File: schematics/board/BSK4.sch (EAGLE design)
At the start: 19 parts

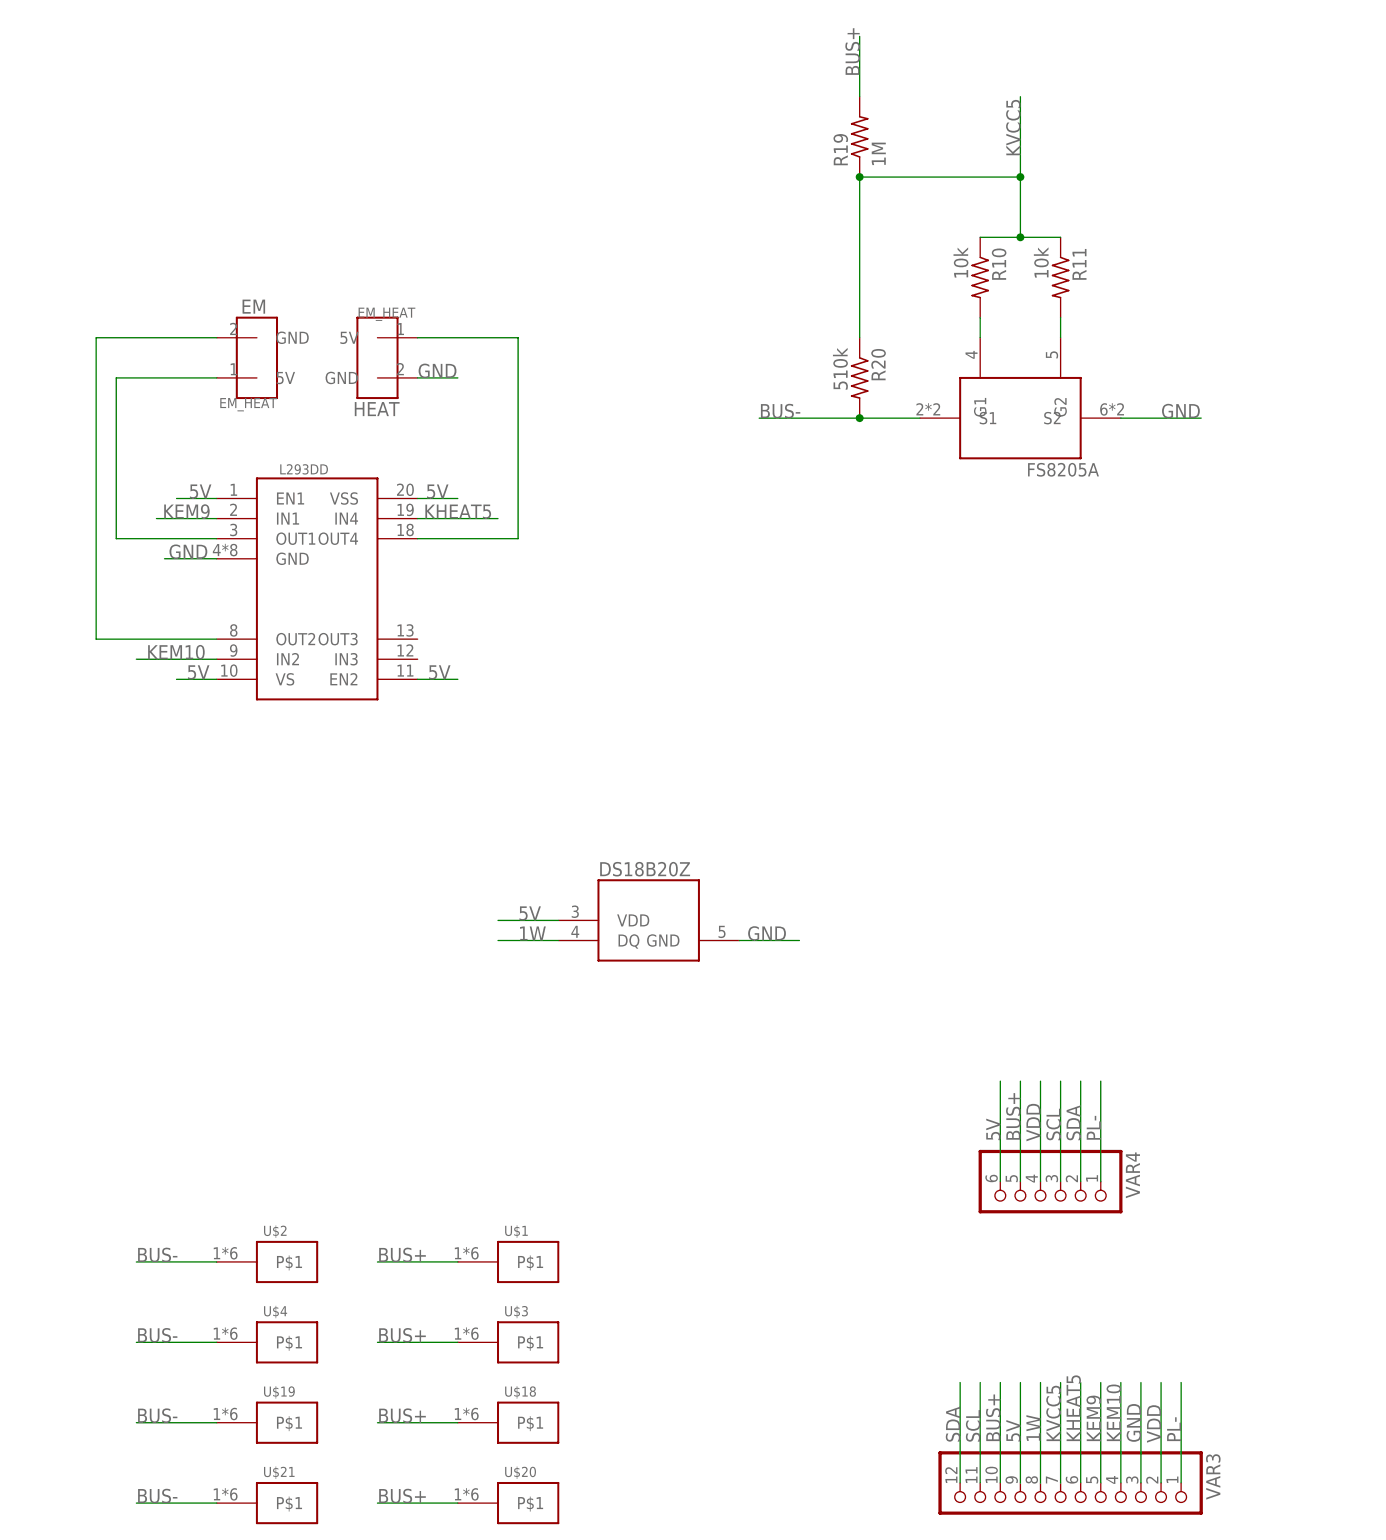
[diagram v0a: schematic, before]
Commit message: изменен БСК4
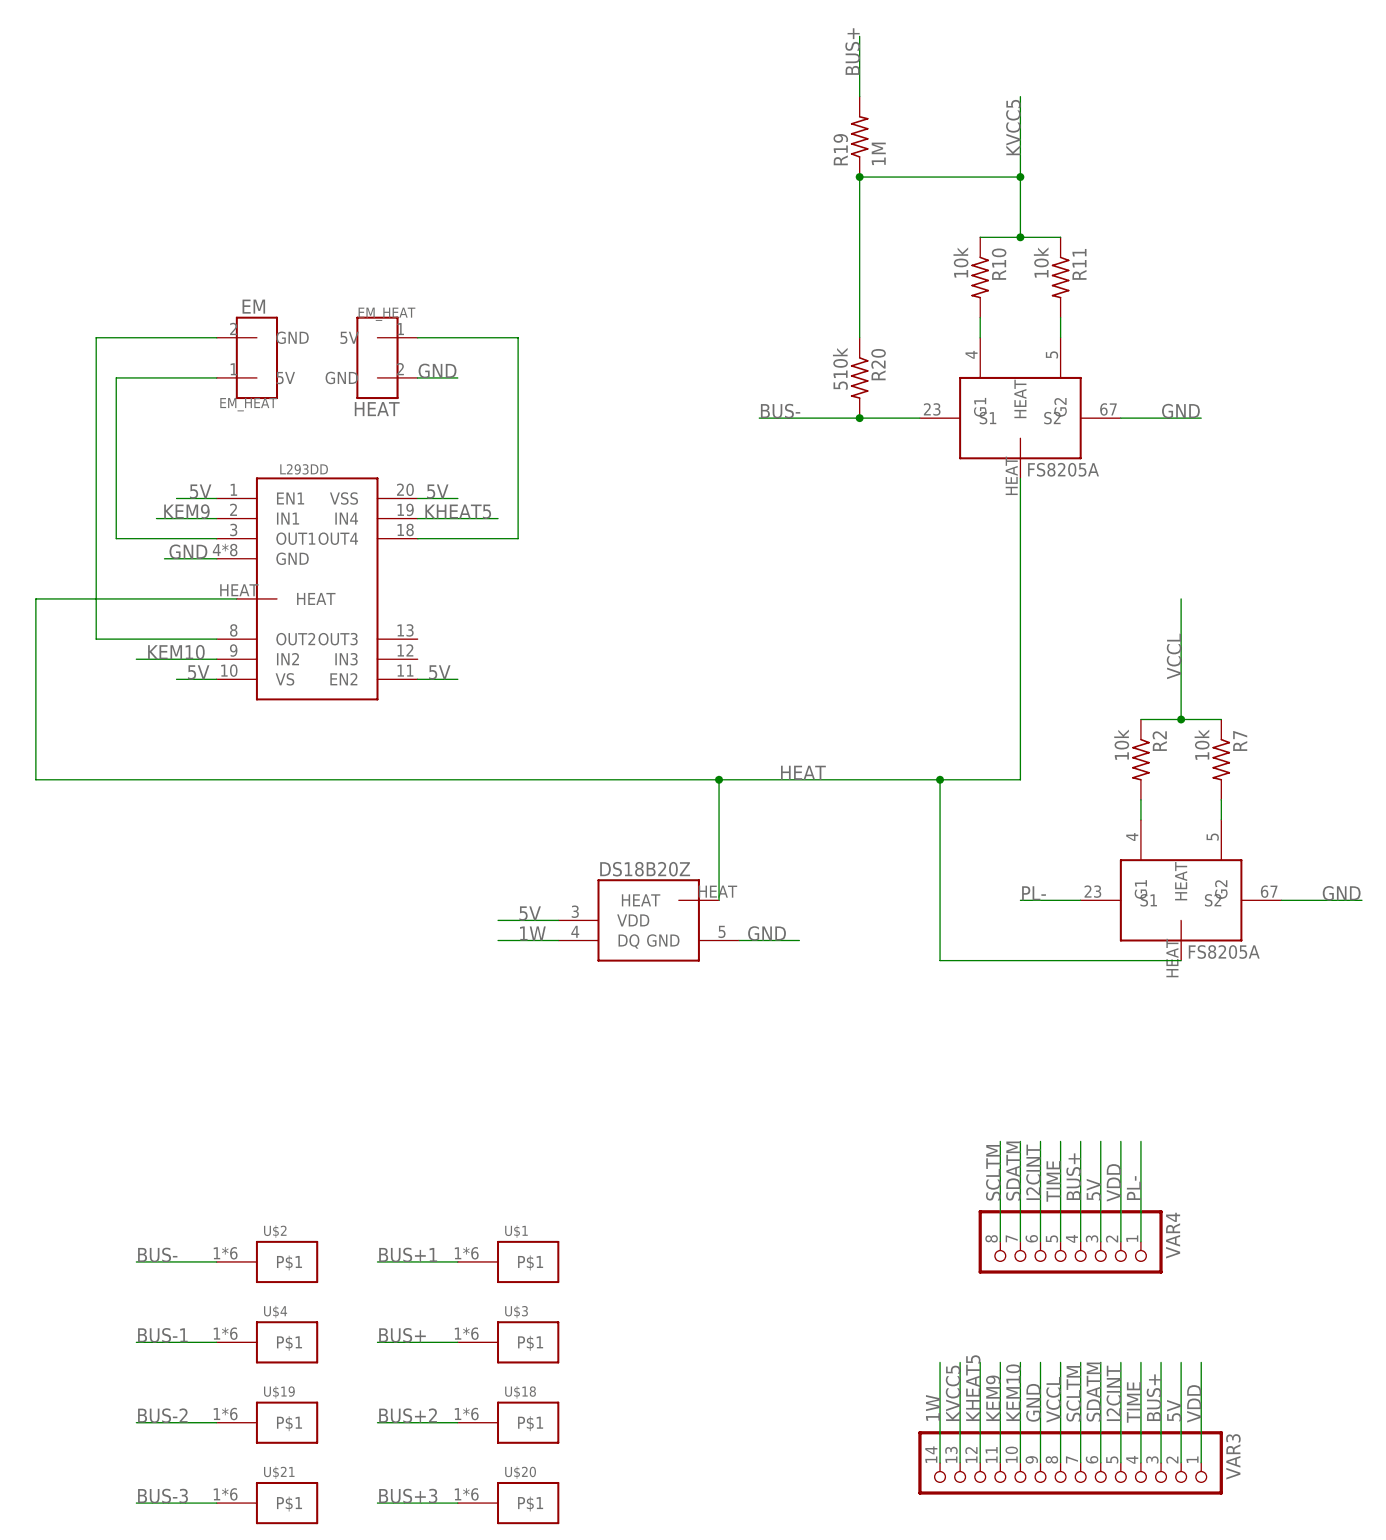
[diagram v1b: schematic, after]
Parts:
- removed U$14: FS8205A, CanCubeSat:FS8205A
- added R2, R7: 10k, resistor:R-US_R0603
- added U$10, U$9: FS8205A+, CanCubeSat:FS8205A+
- U$5: value DS18B20ZDS18B20Z -> DS18B20Z; device CanCubeSat:DS18B20ZDS18B20Z -> CanCubeSat:DS18B20Z
- VAR3: device pinheadCS:PINHD-1X12 -> pinheadCS:PINHD-1X14
- VAR4: device pinheadCS:PINHD-1X6 -> pinheadCS:PINHD-1X8
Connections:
- removed net SCL: VAR3.11, VAR4.3
- removed net SDA: VAR3.12, VAR4.2
- new net BUS+1: U$1.P$1
- new net BUS+2: U$18.P$1
- new net BUS+3: U$20.P$1
- new net BUS-1: U$4.P$1
- new net BUS-2: U$19.P$1
- new net BUS-3: U$21.P$1
- new net HEAT: U$10.HEAT, U$5.HEAT, U$8.HEAT, U$9.HEAT
- new net I2CINT: VAR3.5, VAR4.6
- new net N$4: R2.2, U$10.G1
- new net N$6: R7.2, U$10.G2
- new net SCLTM: VAR3.7, VAR4.8
- new net SDATM: VAR3.6, VAR4.7
- new net TIME: VAR3.4, VAR4.5
- new net VCCL: R2.1, R7.1, VAR3.8
- net 1W: now also VAR3.14; no longer VAR3.8
- net 5V: now also VAR3.2, VAR4.3; no longer VAR3.9, VAR4.6
- net BUS+: now also VAR3.3, VAR4.4; no longer U$1.P$1, U$18.P$1, U$20.P$1, VAR3.10, VAR4.5
- net BUS-: now also U$9.S1; no longer U$14.S1, U$19.P$1, U$21.P$1, U$4.P$1
- net GND: now also U$10.S2, U$9.S2, VAR3.9; no longer U$14.S2, VAR3.3
- net KEM10: now also VAR3.10; no longer VAR3.4
- net KEM9: now also VAR3.11; no longer VAR3.5
- net KHEAT5: now also VAR3.12; no longer VAR3.6
- net KVCC5: now also VAR3.13; no longer VAR3.7
- net N$8: now also U$9.G1; no longer U$14.G1
- net N$9: now also U$9.G2; no longer U$14.G2
- net PL-: now also U$10.S1; no longer VAR3.1
- net VDD: now also VAR3.1, VAR4.2; no longer VAR3.2, VAR4.4

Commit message: Реструктурированы сигналы коммутации для плат БСК
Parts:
- renumbered VAR3 to BSK1, VAR4 to PAYLOAD
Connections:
- net KEM10 renamed B4_KEM-
- net KEM9 renamed B4_KEM+
- net KHEAT5 renamed B4_KHEAT
- net KVCC5 renamed B4_KVCC
- net VCCL renamed PL_KVCC
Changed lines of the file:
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@@
 <part name="R2" library="resistor" library_urn="urn:adsk.eagle:library:348" deviceset="R-US_" device="R0603" package3d_urn="urn:adsk.eagle:package:23555/3" value="10k"/>
 <part name="R7" library="resistor" library_urn="urn:adsk.eagle:library:348" deviceset="R-US_" device="R0603" package3d_urn="urn:adsk.eagle:package:23555/3" value="10k"/>
-<part name="VAR3" library="pinheadCS" deviceset="PINHD-1X14" device=""/>
-<part name="VAR4" library="pinheadCS" deviceset="PINHD-1X8" device=""/>
+<part name="BSK1" library="pinheadCS" deviceset="PINHD-1X14" device=""/>
+<part name="PAYLOAD" library="pinheadCS" deviceset="PINHD-1X8" device=""/>
 <part name="U$10" library="CanCubeSat" deviceset="FS8205A+" device=""/>
 </parts>
@@
 <attribute name="VALUE" x="177.038" y="179.07" size="1.778" layer="96" rot="R270"/>
 </instance>
-<instance part="VAR3" gate="A" x="162.56" y="83.82" smashed="yes" rot="R270">
+<instance part="BSK1" gate="A" x="162.56" y="83.82" smashed="yes" rot="R270">
 <attribute name="NAME" x="180.975" y="90.17" size="1.778" layer="95" rot="R270"/>
 <attribute name="VALUE" x="139.7" y="90.17" size="1.778" layer="96" rot="R270"/>
 </instance>
-<instance part="VAR4" gate="A" x="160.02" y="111.76" smashed="yes" rot="R270">
+<instance part="PAYLOAD" gate="A" x="160.02" y="111.76" smashed="yes" rot="R270">
 <attribute name="NAME" x="173.355" y="118.11" size="1.778" layer="95" rot="R270"/>
 <attribute name="VALUE" x="147.32" y="118.11" size="1.778" layer="96" rot="R270"/>
@@
 <wire x1="157.48" y1="86.36" x2="157.48" y2="99.06" width="0.1524" layer="91"/>
 <label x="157.48" y="91.44" size="1.778" layer="95" rot="R90"/>
-<pinref part="VAR3" gate="A" pin="9"/>
+<pinref part="BSK1" gate="A" pin="9"/>
 </segment>
 <segment>
@@
 <wire x1="175.26" y1="86.36" x2="175.26" y2="99.06" width="0.1524" layer="91"/>
 <label x="175.26" y="91.44" size="1.778" layer="95" rot="R90"/>
-<pinref part="VAR3" gate="A" pin="2"/>
+<pinref part="BSK1" gate="A" pin="2"/>
 </segment>
 <segment>
@@
 <wire x1="165.1" y1="114.3" x2="165.1" y2="127" width="0.1524" layer="91"/>
 <label x="165.1" y="119.38" size="1.778" layer="95" rot="R90"/>
-<pinref part="VAR4" gate="A" pin="3"/>
+<pinref part="PAYLOAD" gate="A" pin="3"/>
 </segment>
 </net>
@@
 <wire x1="144.78" y1="86.36" x2="144.78" y2="99.06" width="0.1524" layer="91"/>
 <label x="144.78" y="91.44" size="1.778" layer="95" rot="R90"/>
-<pinref part="VAR3" gate="A" pin="14"/>
-</segment>
-</net>
-<net name="KEM9" class="0">
+<pinref part="BSK1" gate="A" pin="14"/>
+</segment>
+</net>
+<net name="B4_KEM+" class="0">
 <segment>
 <wire x1="152.4" y1="86.36" x2="152.4" y2="99.06" width="0.1524" layer="91"/>
 <label x="152.4" y="91.44" size="1.778" layer="95" rot="R90"/>
-<pinref part="VAR3" gate="A" pin="11"/>
+<pinref part="BSK1" gate="A" pin="11"/>
 </segment>
 <segment>
@@
 </segment>
 </net>
-<net name="KEM10" class="0">
+<net name="B4_KEM-" class="0">
 <segment>
 <wire x1="154.94" y1="86.36" x2="154.94" y2="99.06" width="0.1524" layer="91"/>
 <label x="154.94" y="91.44" size="1.778" layer="95" rot="R90"/>
-<pinref part="VAR3" gate="A" pin="10"/>
+<pinref part="BSK1" gate="A" pin="10"/>
 </segment>
 <segment>
@@
 </segment>
 </net>
-<net name="KHEAT5" class="0">
+<net name="B4_KHEAT" class="0">
 <segment>
 <wire x1="149.86" y1="86.36" x2="149.86" y2="99.06" width="0.1524" layer="91"/>
 <label x="149.86" y="91.44" size="1.778" layer="95" rot="R90"/>
-<pinref part="VAR3" gate="A" pin="12"/>
+<pinref part="BSK1" gate="A" pin="12"/>
 </segment>
 <segment>
@@
 <wire x1="177.8" y1="86.36" x2="177.8" y2="99.06" width="0.1524" layer="91"/>
 <label x="177.8" y="91.44" size="1.778" layer="95" rot="R90"/>
-<pinref part="VAR3" gate="A" pin="1"/>
+<pinref part="BSK1" gate="A" pin="1"/>
 </segment>
 <segment>
 <wire x1="167.64" y1="114.3" x2="167.64" y2="127" width="0.1524" layer="91"/>
 <label x="167.64" y="119.38" size="1.778" layer="95" rot="R90"/>
-<pinref part="VAR4" gate="A" pin="2"/>
-</segment>
-</net>
-<net name="KVCC5" class="0">
+<pinref part="PAYLOAD" gate="A" pin="2"/>
+</segment>
+</net>
+<net name="B4_KVCC" class="0">
 <segment>
 <wire x1="147.32" y1="86.36" x2="147.32" y2="99.06" width="0.1524" layer="91"/>
 <label x="147.32" y="91.44" size="1.778" layer="95" rot="R90"/>
-<pinref part="VAR3" gate="A" pin="13"/>
+<pinref part="BSK1" gate="A" pin="13"/>
 </segment>
 <segment>
@@
 <wire x1="165.1" y1="86.36" x2="165.1" y2="99.06" width="0.1524" layer="91"/>
 <label x="165.1" y="91.44" size="1.778" layer="95" rot="R90"/>
-<pinref part="VAR3" gate="A" pin="6"/>
+<pinref part="BSK1" gate="A" pin="6"/>
 </segment>
 <segment>
 <wire x1="154.94" y1="114.3" x2="154.94" y2="127" width="0.1524" layer="91"/>
 <label x="154.94" y="119.38" size="1.778" layer="95" rot="R90"/>
-<pinref part="VAR4" gate="A" pin="7"/>
+<pinref part="PAYLOAD" gate="A" pin="7"/>
 </segment>
 </net>
@@
 <wire x1="162.56" y1="86.36" x2="162.56" y2="99.06" width="0.1524" layer="91"/>
 <label x="162.56" y="91.44" size="1.778" layer="95" rot="R90"/>
-<pinref part="VAR3" gate="A" pin="7"/>
+<pinref part="BSK1" gate="A" pin="7"/>
 </segment>
 <segment>
 <wire x1="152.4" y1="114.3" x2="152.4" y2="127" width="0.1524" layer="91"/>
 <label x="152.4" y="119.38" size="1.778" layer="95" rot="R90"/>
-<pinref part="VAR4" gate="A" pin="8"/>
+<pinref part="PAYLOAD" gate="A" pin="8"/>
 </segment>
 </net>
@@
 <wire x1="172.72" y1="86.36" x2="172.72" y2="99.06" width="0.1524" layer="91"/>
 <label x="172.72" y="91.44" size="1.778" layer="95" rot="R90"/>
-<pinref part="VAR3" gate="A" pin="3"/>
+<pinref part="BSK1" gate="A" pin="3"/>
 </segment>
 <segment>
@@
 <wire x1="162.56" y1="114.3" x2="162.56" y2="127" width="0.1524" layer="91"/>
 <label x="162.56" y="119.38" size="1.778" layer="95" rot="R90"/>
-<pinref part="VAR4" gate="A" pin="4"/>
+<pinref part="PAYLOAD" gate="A" pin="4"/>
 </segment>
 </net>
@@
 <wire x1="170.18" y1="114.3" x2="170.18" y2="127" width="0.1524" layer="91"/>
 <label x="170.18" y="119.38" size="1.778" layer="95" rot="R90"/>
-<pinref part="VAR4" gate="A" pin="1"/>
+<pinref part="PAYLOAD" gate="A" pin="1"/>
 </segment>
 <segment>
@@
 </segment>
 </net>
-<net name="VCCL" class="0">
+<net name="PL_KVCC" class="0">
 <segment>
 <pinref part="R2" gate="G$1" pin="1"/>
@@
 <wire x1="160.02" y1="86.36" x2="160.02" y2="99.06" width="0.1524" layer="91"/>
 <label x="160.02" y="91.44" size="1.778" layer="95" rot="R90"/>
-<pinref part="VAR3" gate="A" pin="8"/>
+<pinref part="BSK1" gate="A" pin="8"/>
 </segment>
 </net>
 <net name="I2CINT" class="0">
 <segment>
-<pinref part="VAR3" gate="A" pin="5"/>
+<pinref part="BSK1" gate="A" pin="5"/>
 <wire x1="167.64" y1="86.36" x2="167.64" y2="99.06" width="0.1524" layer="91"/>
 <label x="167.64" y="91.44" size="1.778" layer="95" rot="R90"/>
 </segment>
 <segment>
-<pinref part="VAR4" gate="A" pin="6"/>
+<pinref part="PAYLOAD" gate="A" pin="6"/>
 <wire x1="157.48" y1="114.3" x2="157.48" y2="127" width="0.1524" layer="91"/>
 <label x="157.48" y="119.38" size="1.778" layer="95" rot="R90"/>
@@
 <net name="TIME" class="0">
 <segment>
-<pinref part="VAR3" gate="A" pin="4"/>
+<pinref part="BSK1" gate="A" pin="4"/>
 <wire x1="170.18" y1="86.36" x2="170.18" y2="99.06" width="0.1524" layer="91"/>
 <label x="170.18" y="91.44" size="1.778" layer="95" rot="R90"/>
 </segment>
 <segment>
-<pinref part="VAR4" gate="A" pin="5"/>
+<pinref part="PAYLOAD" gate="A" pin="5"/>
 <wire x1="160.02" y1="114.3" x2="160.02" y2="127" width="0.1524" layer="91"/>
 <label x="160.02" y="119.38" size="1.778" layer="95" rot="R90"/>

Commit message: Добавлены светодиоды на платы БСК
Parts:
- added LED1, LED2, LED3, LED4, LED5: (no value), led:LEDCHIPLED_0603
- added R1, R3, R4, R5, R81: 2k, resistor:R-US_R0603
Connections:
- new net N$10: LED3.C, R3.1
- new net N$27: LED4.C, R4.2
- new net N$28: LED5.C, R5.2
- new net N$5: LED2.C, R81.2
- new net N$7: LED1.A, R1.2
- net 5V: now also R4.1, R5.1
- net BUS-: now also LED4.A
- net GND: now also R3.2
- net N$1: now also LED1.C, LED2.A
- net N$2: now also R1.1, R81.1
- net N$3: now also LED3.A
- net PL-: now also LED5.A
